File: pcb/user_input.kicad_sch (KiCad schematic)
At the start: 10 parts, among them SW2 ENC_SPST_24PPR_PEC12R-4225F-S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

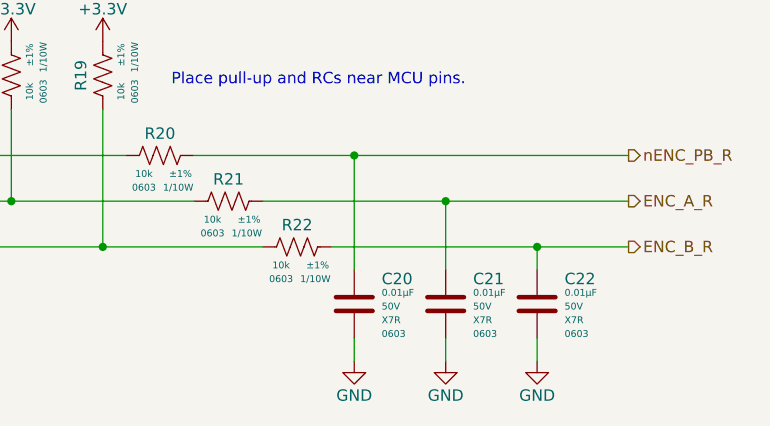
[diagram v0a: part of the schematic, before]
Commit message: Added switch debouncing
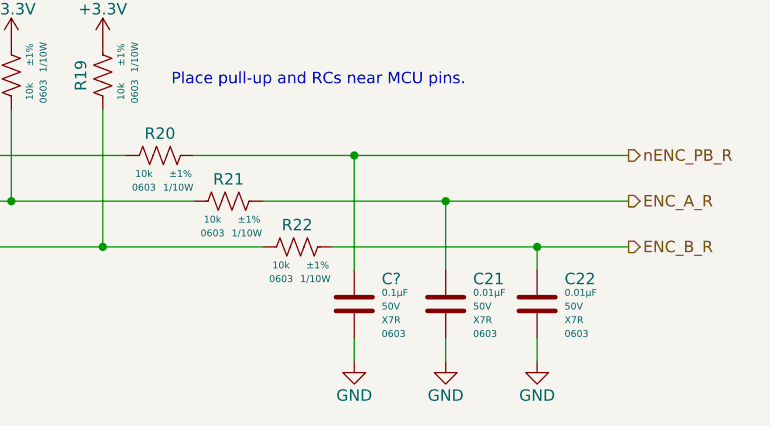
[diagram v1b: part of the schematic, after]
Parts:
- removed C20: CAP_CER_0u01_50V_X7R_0603, Capacitor_SMD:C_0603_1608Metric, symbol arjun_symbols:CAP_CER_0u01_50V_X7R_0603
- added C?: CAP_CER_0u1_50V_X7R_0603, Capacitor_SMD:C_0603_1608Metric, symbol arjun_symbols:CAP_CER_0u1_50V_X7R_0603
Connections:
- net GND: now also C?.2
- net nENC_PB_R: now also C?.1
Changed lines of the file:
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@@
-    (pin "2")
-  )
-  (symbol (lib_id "arjun_symbols:CAP_CER_0u01_50V_X7R_0603") (at 99.06 68.58 0) (unit 1)
-    (in_bom yes) (on_board yes)
-    (property "Reference" "C20" (id 0) (at 102.108 69.596 0)
-      (effects (font (size 1.27 1.27)) (justify left))
-    )
-    (property "Value" "CAP_CER_0u01_50V_X7R_0603" (id 1) (at 106.68 64.135 0)
-      (effects (font (size 1.27 1.27)) (justify left) hide)
-    )
-    (property "Footprint" "Capacitor_SMD:C_0603_1608Metric" (id 2) (at 106.68 66.04 0)
-      (effects (font (size 1.27 1.27)) (justify left) hide)
-    )
-    (property "Datasheet" "https://media.digikey.com/pdf/Data%20Sheets/Samsung%20PDFs/CL10B103KB8NNNC_Spec.pdf" (id 3) (at 106.68 76.2 0)
-      (effects (font (size 1.27 1.27)) (justify left) hide)
-    )
-    (property "Manufacturer" "Samsung Electro-Mechanics" (id 4) (at 106.68 71.12 0)
-      (effects (font (size 1.27 1.27)) (justify left) hide)
-    )
-    (property "ManufacturerPN" "CL10B103KB8NNNC" (id 5) (at 106.68 73.66 0)
-      (effects (font (size 1.27 1.27)) (justify left) hide)
-    )
-    (property "Vendor" "Digi-Key" (id 6) (at 106.68 78.74 0)
-      (effects (font (size 1.27 1.27)) (justify left) hide)
-    )
-    (property "VendorPN" "1276-1009-1-ND" (id 7) (at 106.68 81.28 0)
-      (effects (font (size 1.27 1.27)) (justify left) hide)
-    )
-    (property "Capacitance" "0.01µF" (id 8) (at 102.108 71.12 0)
-      (effects (font (size 0.762 0.762)) (justify left))
-    )
-    (property "Voltage" "50V" (id 9) (at 102.108 72.644 0)
-      (effects (font (size 0.762 0.762)) (justify left))
-    )
-    (property "Package" "0603" (id 10) (at 102.108 75.692 0)
-      (effects (font (size 0.762 0.762)) (justify left))
-    )
-    (property "Temp Co" "X7R" (id 11) (at 102.108 74.168 0)
-      (effects (font (size 0.762 0.762)) (justify left))
-    )
-    (pin "1")
     (pin "2")
   )
@@
     )
     (pin "1")
+    (pin "2")
+  )
+  (symbol (lib_id "arjun_symbols:CAP_CER_0u1_50V_X7R_0603") (at 99.06 68.58 0) (unit 1)
+    (in_bom yes) (on_board yes)
+    (property "Reference" "C?" (id 0) (at 102.108 69.596 0)
+      (effects (font (size 1.27 1.27)) (justify left))
+    )
+    (property "Value" "CAP_CER_0u1_50V_X7R_0603" (id 1) (at 106.68 64.135 0)
+      (effects (font (size 1.27 1.27)) (justify left) hide)
+    )
+    (property "Footprint" "Capacitor_SMD:C_0603_1608Metric" (id 2) (at 106.68 66.04 0)
+      (effects (font (size 1.27 1.27)) (justify left) hide)
+    )
+    (property "Datasheet" "https://media.digikey.com/pdf/Data%20Sheets/Samsung%20PDFs/CL10B104KB8NNNC_Spec.pdf" (id 3) (at 106.68 76.2 0)
+      (effects (font (size 1.27 1.27)) (justify left) hide)
+    )
+    (property "Manufacturer" "Samsung Electro-Mechanics" (id 4) (at 106.68 71.12 0)
+      (effects (font (size 1.27 1.27)) (justify left) hide)
+    )
+    (property "ManufacturerPN" "CL10B104KB8NNNC" (id 5) (at 106.68 73.66 0)
+      (effects (font (size 1.27 1.27)) (justify left) hide)
+    )
+    (property "Vendor" "Digi-Key" (id 6) (at 106.68 78.74 0)
+      (effects (font (size 1.27 1.27)) (justify left) hide)
+    )
+    (property "VendorPN" "1276-1000-1-ND" (id 7) (at 106.68 81.28 0)
+      (effects (font (size 1.27 1.27)) (justify left) hide)
+    )
+    (property "Capacitance" "0.1µF" (id 8) (at 102.108 71.12 0)
+      (effects (font (size 0.762 0.762)) (justify left))
+    )
+    (property "Voltage" "50V" (id 9) (at 102.108 72.644 0)
+      (effects (font (size 0.762 0.762)) (justify left))
+    )
+    (property "Package" "0603" (id 10) (at 102.108 75.692 0)
+      (effects (font (size 0.762 0.762)) (justify left))
+    )
+    (property "Temp Co" "X7R" (id 11) (at 102.108 74.168 0)
+      (effects (font (size 0.762 0.762)) (justify left))
+    )
+    (pin "1")

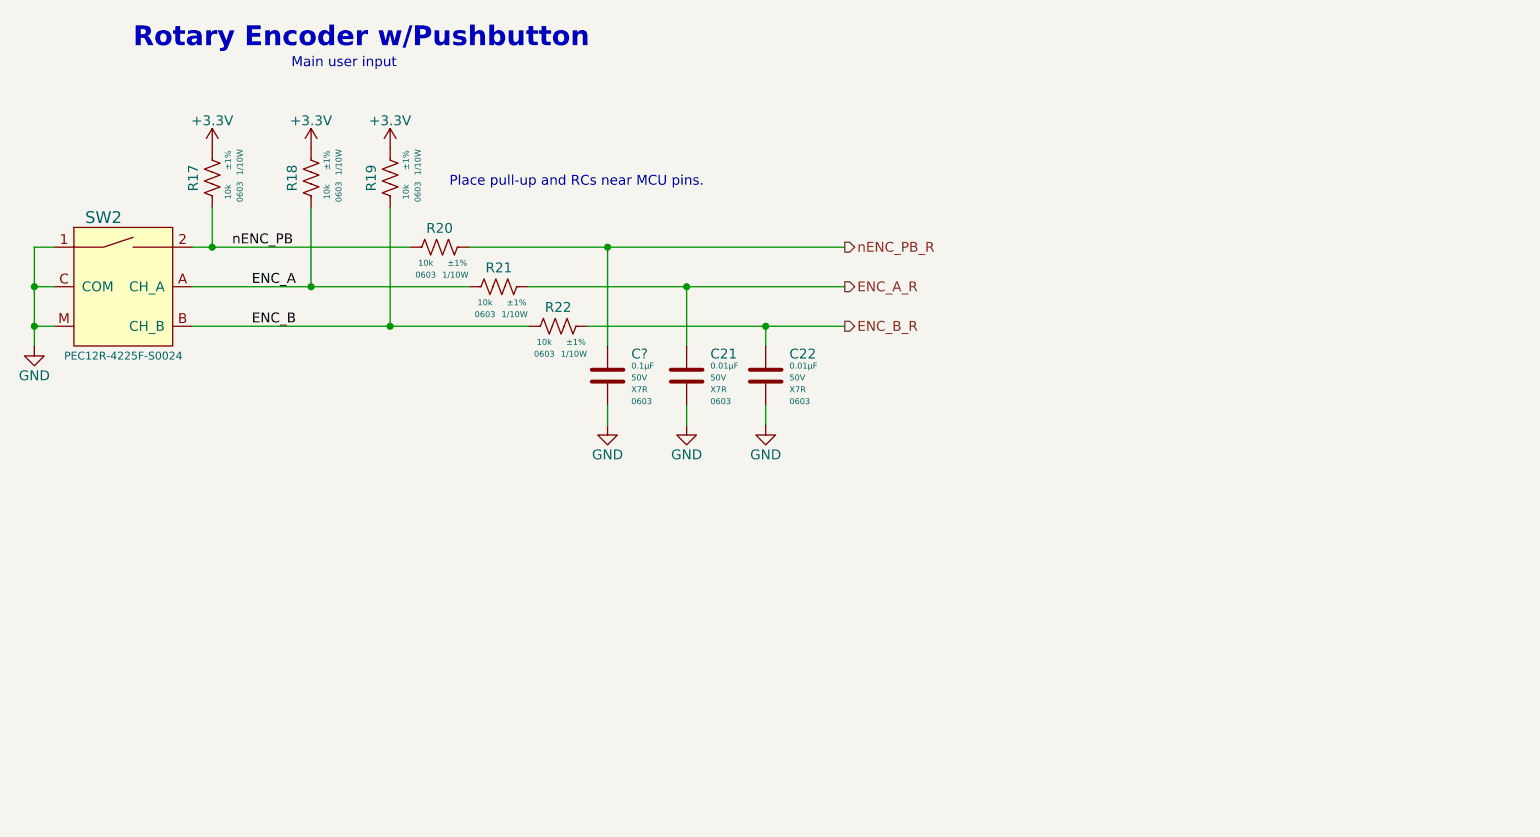
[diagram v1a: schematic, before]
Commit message: Added MCU pinouts for rotary encoder
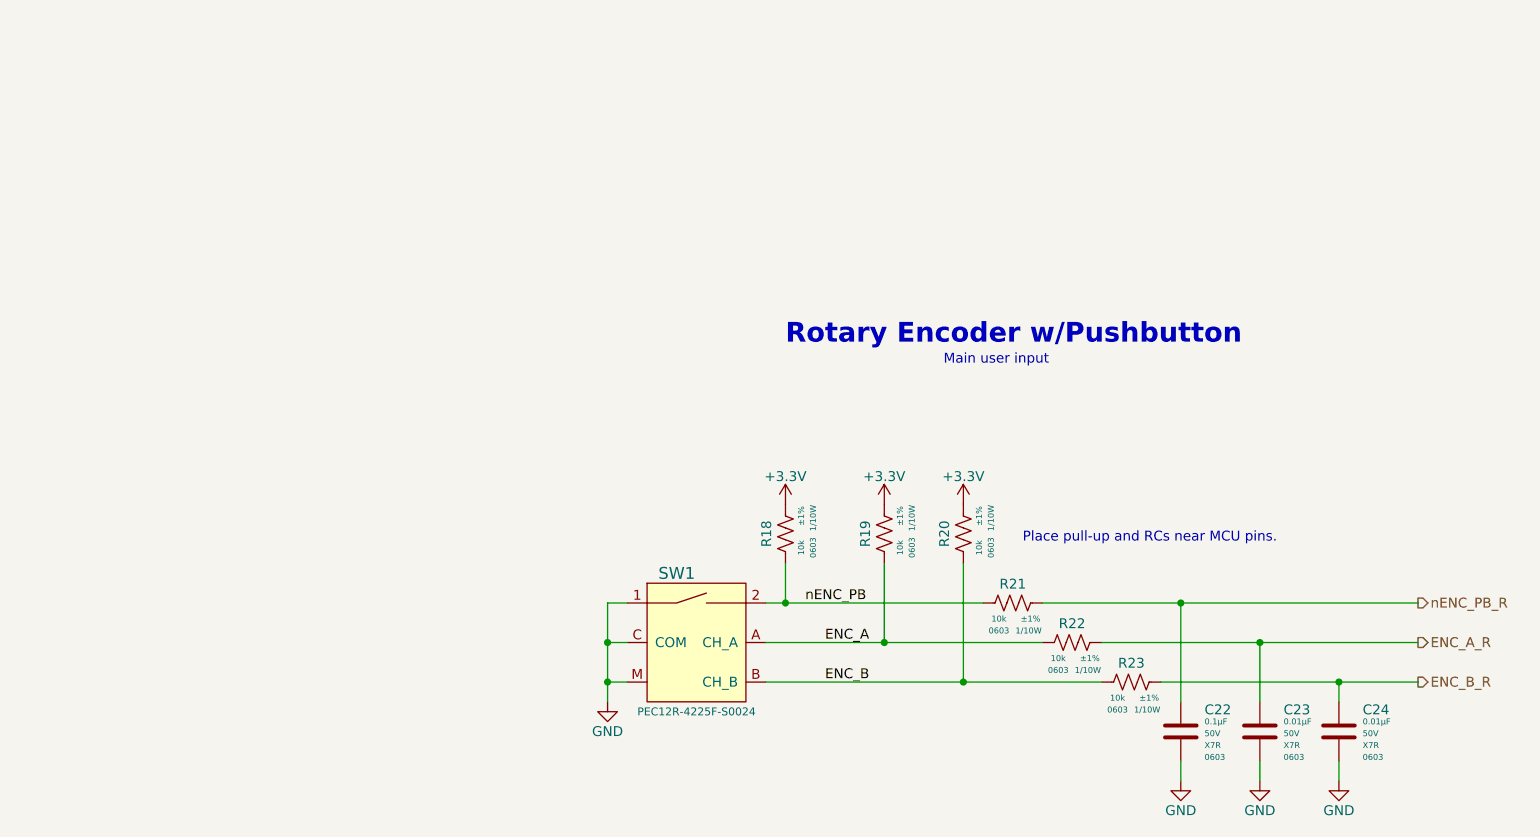
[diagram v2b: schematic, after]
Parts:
- gave numbers to parts that had none: 1
- renumbered C21 to C23, C22 to C24, R17 to R18, R18 to R19, R19 to R20, R20 to R21, R21 to R22, R22 to R23, SW2 to SW1
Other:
- moved on the sheet: C22, C23, C24, R18, R19, R20, R21, R22, R23, SW1

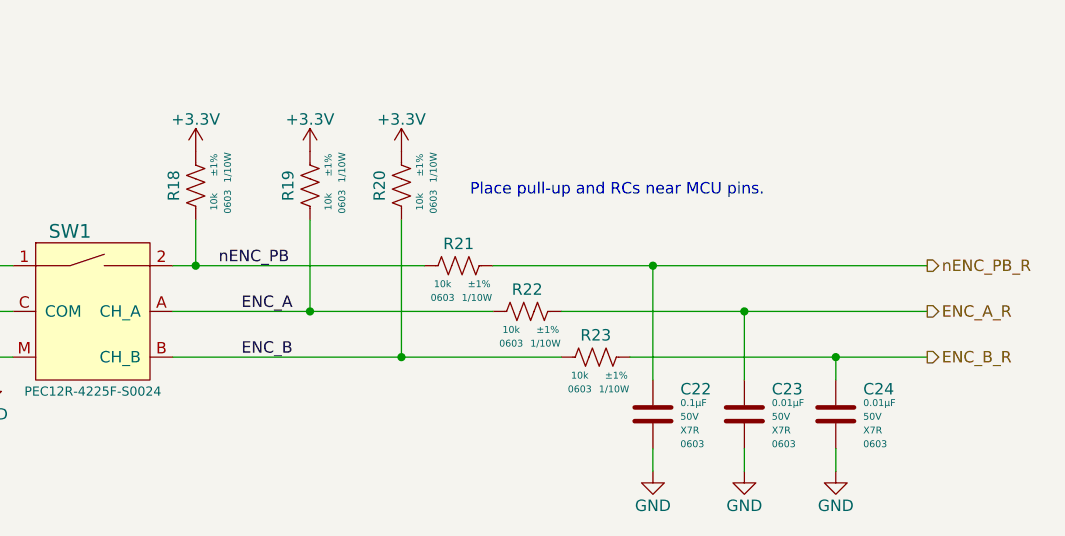
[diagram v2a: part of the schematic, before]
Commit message: Added snubber DNP footprints and named nets on power page.
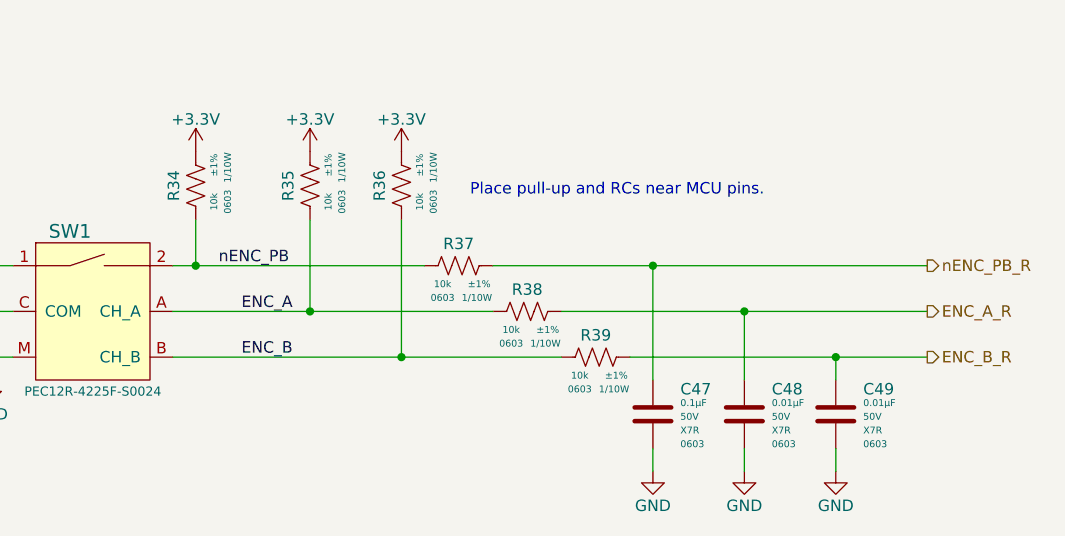
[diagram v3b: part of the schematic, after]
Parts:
- renumbered C22 to C47, C23 to C48, C24 to C49, R18 to R34, R19 to R35, R20 to R36, R21 to R37, R22 to R38, R23 to R39
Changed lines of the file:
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@@
   (symbol (lib_id "power:GND") (at 172.72 124.46 0) (unit 1)
     (in_bom yes) (on_board yes)
-    (property "Reference" "#PWR052" (id 0) (at 172.72 130.81 0)
+    (property "Reference" "#PWR074" (id 0) (at 172.72 130.81 0)
       (effects (font (size 1.27 1.27)) hide)
     )
@@
   (symbol (lib_id "arjun_symbols:RES_10K_1P_1{slash}10W_0603") (at 162.56 106.68 270) (unit 1)
     (in_bom yes) (on_board yes)
-    (property "Reference" "R22" (id 0) (at 158.75 103.505 90)
+    (property "Reference" "R38" (id 0) (at 158.75 103.505 90)
       (effects (font (size 1.27 1.27)) (justify top))
     )
@@
   (symbol (lib_id "power:GND") (at 182.88 124.46 0) (unit 1)
     (in_bom yes) (on_board yes)
-    (property "Reference" "#PWR053" (id 0) (at 182.88 130.81 0)
+    (property "Reference" "#PWR075" (id 0) (at 182.88 130.81 0)
       (effects (font (size 1.27 1.27)) hide)
     )
@@
   (symbol (lib_id "arjun_symbols:CAP_CER_0u01_50V_X7R_0603") (at 193.04 114.3 0) (unit 1)
     (in_bom yes) (on_board yes)
-    (property "Reference" "C24" (id 0) (at 196.088 115.316 0)
+    (property "Reference" "C49" (id 0) (at 196.088 115.316 0)
       (effects (font (size 1.27 1.27)) (justify left))
     )
@@
   (symbol (lib_id "power:GND") (at 193.04 124.46 0) (unit 1)
     (in_bom yes) (on_board yes)
-    (property "Reference" "#PWR054" (id 0) (at 193.04 130.81 0)
+    (property "Reference" "#PWR076" (id 0) (at 193.04 130.81 0)
       (effects (font (size 1.27 1.27)) hide)
     )
@@
   (symbol (lib_id "arjun_symbols:RES_10K_1P_1{slash}10W_0603") (at 134.62 88.9 0) (unit 1)
     (in_bom yes) (on_board yes)
-    (property "Reference" "R19" (id 0) (at 131.445 92.71 90)
+    (property "Reference" "R35" (id 0) (at 131.445 92.71 90)
       (effects (font (size 1.27 1.27)) (justify top))
     )
@@
   (symbol (lib_id "power:+3.3V") (at 134.62 88.9 0) (unit 1)
     (in_bom yes) (on_board yes)
-    (property "Reference" "#PWR050" (id 0) (at 134.62 92.71 0)
+    (property "Reference" "#PWR072" (id 0) (at 134.62 92.71 0)
       (effects (font (size 1.27 1.27)) hide)
     )
@@
   (symbol (lib_id "arjun_symbols:RES_10K_1P_1{slash}10W_0603") (at 144.78 88.9 0) (unit 1)
     (in_bom yes) (on_board yes)
-    (property "Reference" "R20" (id 0) (at 141.605 92.71 90)
+    (property "Reference" "R36" (id 0) (at 141.605 92.71 90)
       (effects (font (size 1.27 1.27)) (justify top))
     )
@@
   (symbol (lib_id "arjun_symbols:RES_10K_1P_1{slash}10W_0603") (at 154.94 101.6 270) (unit 1)
     (in_bom yes) (on_board yes)
-    (property "Reference" "R21" (id 0) (at 151.13 98.425 90)
+    (property "Reference" "R37" (id 0) (at 151.13 98.425 90)
       (effects (font (size 1.27 1.27)) (justify top))
     )
@@
   (symbol (lib_id "arjun_symbols:RES_10K_1P_1{slash}10W_0603") (at 170.18 111.76 270) (unit 1)
     (in_bom yes) (on_board yes)
-    (property "Reference" "R23" (id 0) (at 166.37 108.585 90)
+    (property "Reference" "R39" (id 0) (at 166.37 108.585 90)
       (effects (font (size 1.27 1.27)) (justify top))
     )
@@
   (symbol (lib_id "arjun_symbols:CAP_CER_0u01_50V_X7R_0603") (at 182.88 114.3 0) (unit 1)
     (in_bom yes) (on_board yes)
-    (property "Reference" "C23" (id 0) (at 185.928 115.316 0)
+    (property "Reference" "C48" (id 0) (at 185.928 115.316 0)
       (effects (font (size 1.27 1.27)) (justify left))
     )
@@
   (symbol (lib_id "arjun_symbols:RES_10K_1P_1{slash}10W_0603") (at 121.92 88.9 0) (unit 1)
     (in_bom yes) (on_board yes)
-    (property "Reference" "R18" (id 0) (at 118.745 92.71 90)
+    (property "Reference" "R34" (id 0) (at 118.745 92.71 90)
       (effects (font (size 1.27 1.27)) (justify top))
     )
@@
   (symbol (lib_id "arjun_symbols:CAP_CER_0u1_50V_X7R_0603") (at 172.72 114.3 0) (unit 1)
     (in_bom yes) (on_board yes)
-    (property "Reference" "C22" (id 0) (at 175.768 115.316 0)
+    (property "Reference" "C47" (id 0) (at 175.768 115.316 0)
       (effects (font (size 1.27 1.27)) (justify left))
     )
@@
   (symbol (lib_id "power:GND") (at 99.06 114.3 0) (unit 1)
     (in_bom yes) (on_board yes)
-    (property "Reference" "#PWR048" (id 0) (at 99.06 120.65 0)
+    (property "Reference" "#PWR070" (id 0) (at 99.06 120.65 0)
       (effects (font (size 1.27 1.27)) hide)
     )
@@
   (symbol (lib_id "power:+3.3V") (at 121.92 88.9 0) (unit 1)
     (in_bom yes) (on_board yes)
-    (property "Reference" "#PWR049" (id 0) (at 121.92 92.71 0)
+    (property "Reference" "#PWR071" (id 0) (at 121.92 92.71 0)
       (effects (font (size 1.27 1.27)) hide)
     )
@@
   (symbol (lib_id "power:+3.3V") (at 144.78 88.9 0) (unit 1)
     (in_bom yes) (on_board yes)
-    (property "Reference" "#PWR051" (id 0) (at 144.78 92.71 0)
-      (effects (font (size 1.27 1.27)) hide)
-    )
+    (property "Reference" "#PWR073" (id 0) (at 144.78 92.71 0)
+      (effects (font (size 1.27 1.27)) hide)
+    )

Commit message: Started layout!! 180V boost mostly laid out
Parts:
- R34, R35, R36, R37, R38, R39: symbol arjun_symbols:RES_10K_1P_1/10W_0603 -> arjun_symbols:RES_10K_1P_1/10W_0603
